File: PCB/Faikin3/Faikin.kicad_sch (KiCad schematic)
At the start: 28 parts, among them J1 1x5, J2 Prog, Q3 PMF250XNEX, U1 ESP32-PICO-MINI-02, U3 MD8942, U4 Barcode

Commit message: Fix RGB
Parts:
- D2: symbol Device:LED_RBGA -> Device:LED_RGBA
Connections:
- net at R12.1: now also D2.3 (BK); no longer D2.2 (BK)
- net at R6.1: now also D2.2 (GK); no longer D2.3 (GK)
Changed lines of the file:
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@@
     )
   )
-  (symbol (lib_id "Device:LED_RBGA") (at 66.675 139.065 0) (unit 1)
+  (symbol (lib_id "Device:LED_RGBA") (at 66.675 139.065 0) (unit 1)
     (in_bom yes) (on_board yes) (dnp no)
     (property "Reference" "D2" (at 66.675 126.4412 0)

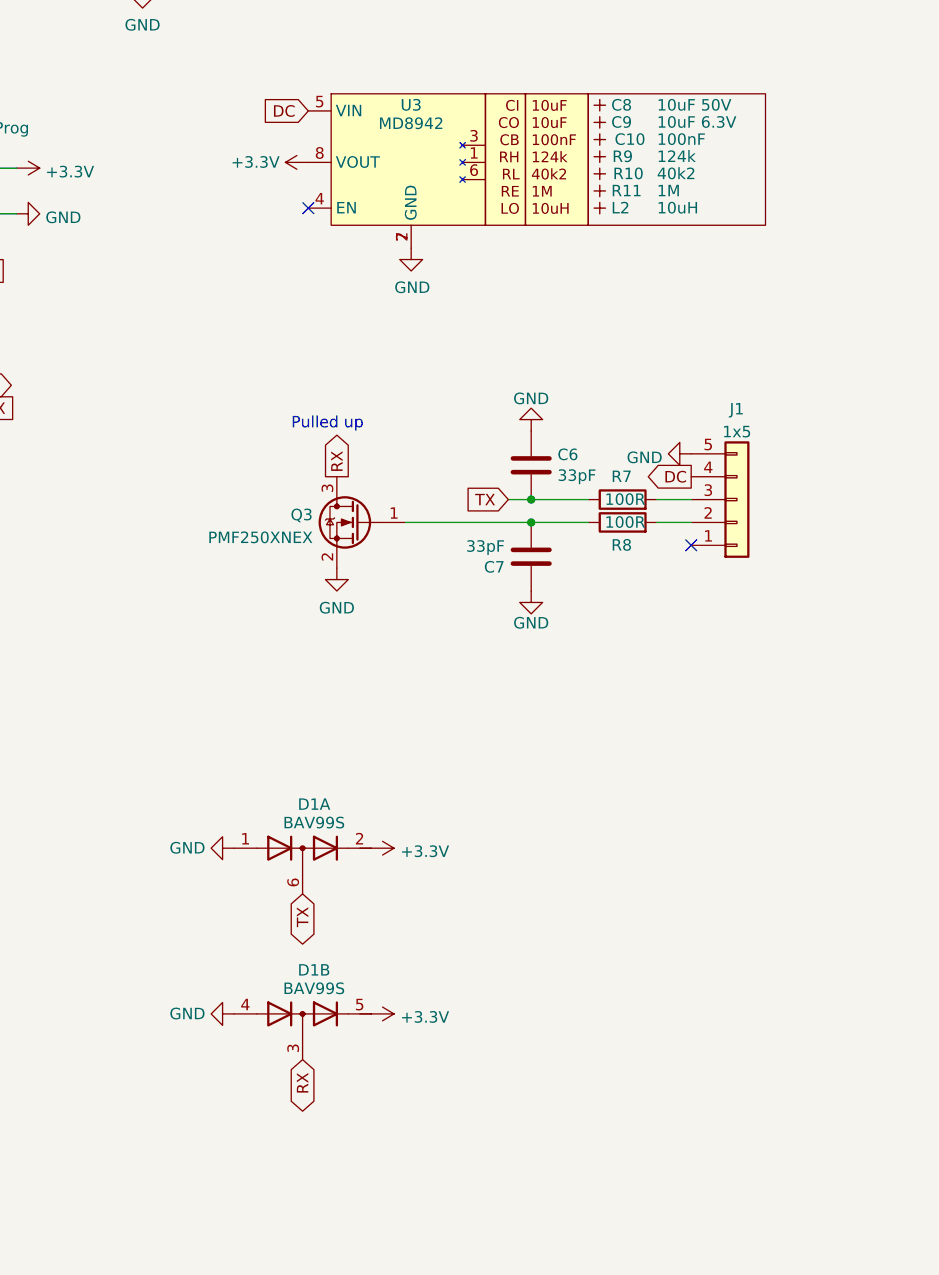
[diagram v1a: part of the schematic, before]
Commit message: Changed to open collector output
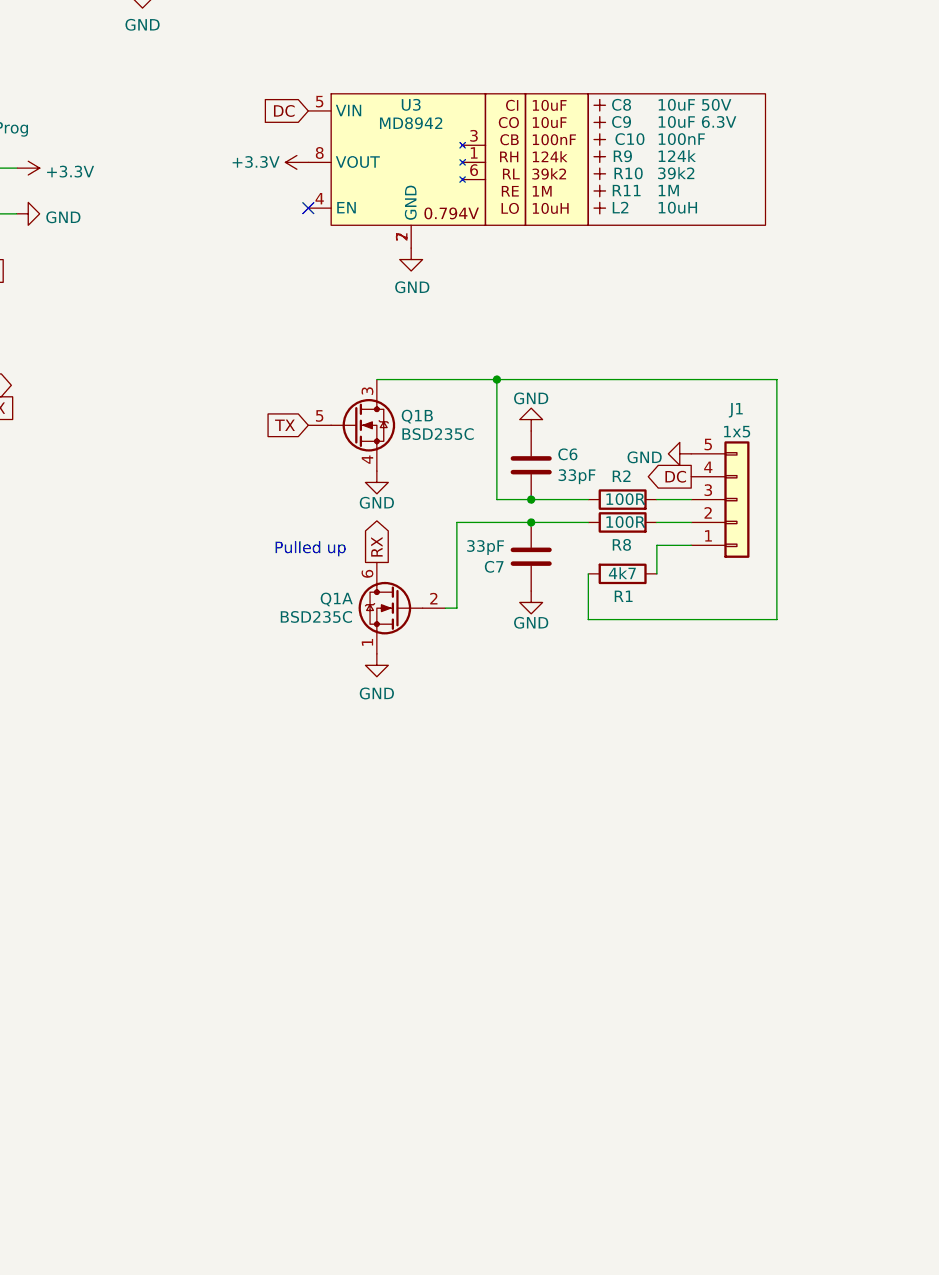
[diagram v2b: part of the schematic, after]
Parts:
- removed D1: BAV99S, RevK:SOT-363_SC-70-6, symbol Diode:BAV99S
- removed Q3: PMF250XNEX, RevK:SOT-323_SC-70, symbol RevK:NX7002AK
- removed R7: 100R, RevK:R_0402, symbol Device:R
- added Q1: BSD235C, RevK:SOT-363_SC-70-6, symbol RevK:BSS138PS
- added R1: 4k7, RevK:R_0402, symbol Device:R
- added R2: 100R, RevK:R_0402, symbol Device:R
- R10: value 40k2 -> 39k2
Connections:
- net GND: now also Q1.1 (SN), Q1.4 (DP)
- net RX: now also Q1.6 (DN)
- net TX: now also Q1.5 (GP); no longer C6.2
- net at C7.2, R8.1: now also Q1.2 (GN)
- net at J1.3 (Pin_3): now also R2.2
- net at J1.1 (Pin_1): now also R1.1
- new net: C6.2, Q1.3 (SP), R1.2, R2.1
- no-connect marks 21 -> 20

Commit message: Fix FET
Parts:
- Q1: value BSD235C -> BSS138PS; JLCPCB Rotation Offset (none) -> 90; LCSC Part # (none) -> C193381
- Q1: value BSD235C -> BSS138PS; LCSC Part # (none) -> C193381
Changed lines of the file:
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@@
       (effects (font (size 1.27 1.27)) (justify left))
     )
-    (property "Value" "BSD235C" (at 129.032 81.669 0)
+    (property "Value" "BSS138PS" (at 129.032 81.669 0)
       (effects (font (size 1.27 1.27)) (justify left))
     )
@@
     (property "Datasheet" "https://datasheet.lcsc.com/lcsc/1810011113_Nexperia-BSS138PS-115_C193381.pdf" (at 123.825 67.31 0)
       (effects (font (size 1.27 1.27)) hide)
+    )
+    (property "LCSC Part #" "C193381" (at 133.35 74.676 0)
+      (effects (font (size 1.27 1.27)) hide)
+    )
+    (property "JLCPCB Rotation Offset" "90" (at 123.825 80.645 0)
+      (effects (font (size 1.27 1.27)))
     )
     (pin "1")
@@
       (effects (font (size 1.27 1.27)) (justify left))
     )
-    (property "Value" "BSD235C" (at 123.698 101.989 0)
+    (property "Value" "BSS138PS" (at 123.698 101.989 0)
       (effects (font (size 1.27 1.27)) (justify left))
     )
@@
       (effects (font (size 1.27 1.27)) hide)
     )
+    (property "LCSC Part #" "C193381" (at 119.38 94.996 0)
+      (effects (font (size 1.27 1.27)) hide)
+    )

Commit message: Silk tidy
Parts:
- removed U4: Barcode, RevK:EAN-5060634238151, symbol RevK:Barcode
- added C2: 100nF, RevK:C_0402, symbol Device:C
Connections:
- net +3.3V: now also C2.1
- net GND: now also C2.2
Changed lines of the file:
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@@
     )
   )
-  (symbol (lib_id "RevK:Barcode") (at 273.05 174.625 0) (unit 1)
-    (in_bom no) (on_board yes) (dnp no) (fields_autoplaced)
-    (property "Reference" "U4" (at 273.05 177.8 0)
-      (effects (font (size 1.27 1.27)) hide)
-    )
-    (property "Value" "Barcode" (at 273.05 179.705 0)
-      (effects (font (size 1.27 1.27)) hide)
-    )
-    (property "Footprint" "RevK:EAN-5060634238151" (at 272.415 175.26 0)
-      (effects (font (size 1.27 1.27)) hide)
-    )
-    (property "Datasheet" "" (at 272.415 175.26 0)
-      (effects (font (size 1.27 1.27)) hide)
-    )
-    (property "Note" "Non part, PCB printed" (at 273.05 168.91 0)
-      (effects (font (size 1.27 1.27)) hide)
-    )
-    (instances
-      (project "Faikin"
-        (path "/46c350bb-7de4-4e81-aafd-4af55e37aab0"
-          (reference "U4") (unit 1)
+  (symbol (lib_id "Device:C") (at 99.695 72.39 0) (unit 1)
+    (in_bom yes) (on_board yes) (dnp no) (fields_autoplaced)
+    (property "Reference" "C2" (at 102.616 71.5553 0)
+      (effects (font (size 1.27 1.27)) (justify left))
+    )
+    (property "Value" "100nF" (at 102.616 74.0922 0)
+      (effects (font (size 1.27 1.27)) (justify left))
+    )
+    (property "Footprint" "RevK:C_0402" (at 100.6602 76.2 0)
+      (effects (font (size 1.27 1.27)) hide)
+    )
+    (property "Datasheet" "~" (at 99.695 72.39 0)
+      (effects (font (size 1.27 1.27)) hide)
+    )
+    (pin "1")
+    (pin "2")
+    (instances
+      (project "Faikin"
+        (path "/46c350bb-7de4-4e81-aafd-4af55e37aab0"
+          (reference "C2") (unit 1)
         )
       )
@@
         (path "/46c350bb-7de4-4e81-aafd-4af55e37aab0"
           (reference "Q1") (unit 2)
+        )
+      )
+    )
+  )
+  (symbol (lib_id "power:GND") (at 99.695 76.2 0) (unit 1)
+    (in_bom yes) (on_board yes) (dnp no) (fields_autoplaced)
+    (property "Reference" "#PWR05" (at 99.695 82.55 0)
+      (effects (font (size 1.27 1.27)) hide)
+    )
+    (property "Value" "GND" (at 99.695 80.6434 0)
+      (effects (font (size 1.27 1.27)))
+    )
+    (property "Footprint" "" (at 99.695 76.2 0)
+      (effects (font (size 1.27 1.27)) hide)
+    )
+    (property "Datasheet" "" (at 99.695 76.2 0)
+      (effects (font (size 1.27 1.27)) hide)
+    )
+    (pin "1")
+    (instances
+      (project "Faikin"
+        (path "/46c350bb-7de4-4e81-aafd-4af55e37aab0"
+          (reference "#PWR05") (unit 1)
         )
       )
@@
         )
       )
+    )
+  )
+  (symbol (lib_id "power:+3.3V") (at 99.695 68.58 0) (unit 1)
+    (in_bom yes) (on_board yes) (dnp no) (fields_autoplaced)
+    (property "Reference" "#PWR04" (at 99.695 72.39 0)
+      (effects (font (size 1.27 1.27)) hide)
+    )
+    (property "Value" "+3.3V" (at 99.695 65.0042 0)
+      (effects (font (size 1.27 1.27)))
+    )
+    (property "Footprint" "" (at 99.695 68.58 0)
+      (effects (font (size 1.27 1.27)) hide)
+    )
+    (property "Datasheet" "" (at 99.695 68.58 0)
+      (effects (font (size 1.27 1.27)) hide)
+    )
+    (pin "1")
+    (instances
+      (project "Faikin"
+        (path "/46c350bb-7de4-4e81-aafd-4af55e37aab0"
+          (reference "#PWR04") (unit 1)
+        )
+      )

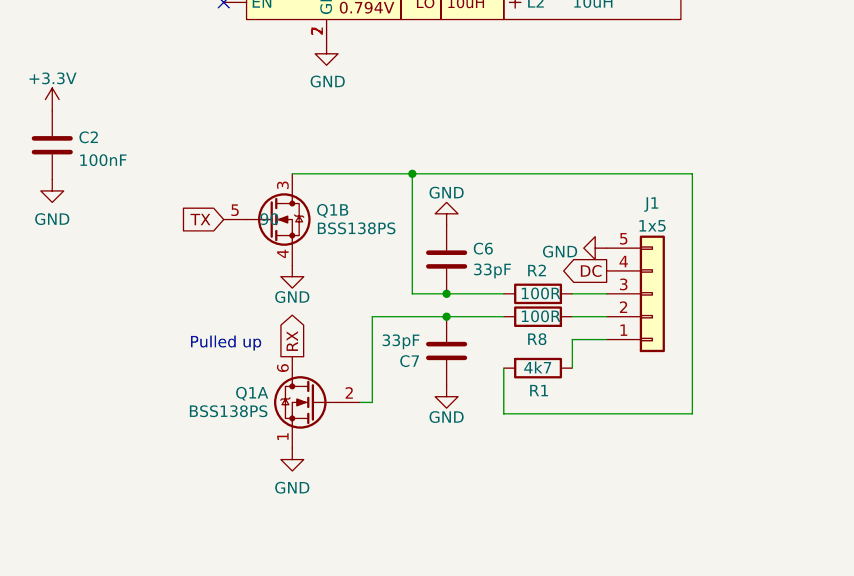
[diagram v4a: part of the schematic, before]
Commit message: Exrta pull up
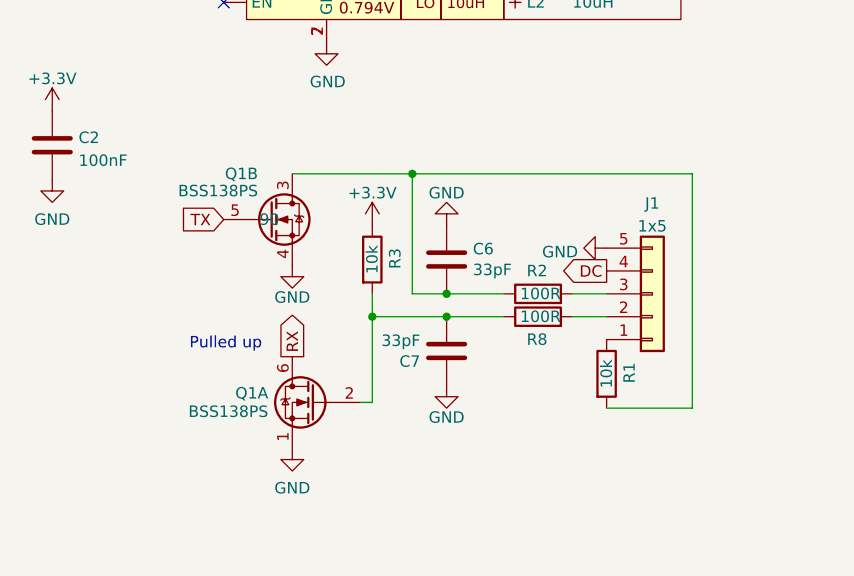
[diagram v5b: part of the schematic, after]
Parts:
- added R3: 10k, RevK:R_0402, symbol Device:R
- R1: value 4k7 -> 10k
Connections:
- net +3.3V: now also R3.1
- net at C7.2, Q1.2 (GN), R8.1: now also R3.2
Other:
- moved on the sheet: R1
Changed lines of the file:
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@@
   (junction (at 81.28 52.07) (diameter 0) (color 0 0 0 0)
+  )
+  (junction (at 135.255 91.44) (diameter 0) (color 0 0 0 0)
   )
   (junction (at 139.7 75.565) (diameter 0) (color 0 0 0 0)
@@
     (stroke (width 0) (type default))
   )
-  (wire (pts (xy 170.815 102.235) (xy 149.86 102.235))
-    (stroke (width 0) (type default))
-  )
   (wire (pts (xy 143.51 91.44) (xy 149.86 91.44))
     (stroke (width 0) (type default))
@@
     (stroke (width 0) (type default))
   )
-  (wire (pts (xy 161.29 93.98) (xy 157.48 93.98))
-    (stroke (width 0) (type default))
-  )
   (wire (pts (xy 126.365 75.565) (xy 139.7 75.565))
     (stroke (width 0) (type default))
@@
     (stroke (width 0) (type default))
   )
-  (wire (pts (xy 135.255 100.965) (xy 135.255 91.44))
-    (stroke (width 0) (type default))
-  )
-  (wire (pts (xy 149.86 102.235) (xy 149.86 97.155))
+  (wire (pts (xy 135.255 91.44) (xy 135.255 100.965))
+    (stroke (width 0) (type default))
+  )
+  (wire (pts (xy 161.29 101.6) (xy 170.815 101.6))
     (stroke (width 0) (type default))
   )
@@
     (stroke (width 0) (type default))
   )
-  (wire (pts (xy 170.815 75.565) (xy 170.815 102.235))
+  (wire (pts (xy 170.815 75.565) (xy 170.815 101.6))
     (stroke (width 0) (type default))
   )
@@
     (stroke (width 0) (type default))
   )
+  (wire (pts (xy 135.255 88.9) (xy 135.255 91.44))
+    (stroke (width 0) (type default))
+  )
   (wire (pts (xy 135.255 91.44) (xy 143.51 91.44))
     (stroke (width 0) (type default))
@@
   )
   (wire (pts (xy 143.51 88.9) (xy 149.86 88.9))
-    (stroke (width 0) (type default))
-  )
-  (wire (pts (xy 157.48 93.98) (xy 157.48 97.155))
     (stroke (width 0) (type default))
   )
@@
   )
   (symbol (lib_name "BSS138PS_1") (lib_id "RevK:BSS138PS") (at 123.825 80.645 0) (unit 2)
-    (in_bom yes) (on_board yes) (dnp no) (fields_autoplaced)
-    (property "Reference" "Q1" (at 129.032 79.621 0)
-      (effects (font (size 1.27 1.27)) (justify left))
-    )
-    (property "Value" "BSS138PS" (at 129.032 81.669 0)
-      (effects (font (size 1.27 1.27)) (justify left))
+    (in_bom yes) (on_board yes) (dnp no)
+    (property "Reference" "Q1" (at 122.555 75.565 0)
+      (effects (font (size 1.27 1.27)) (justify right))
+    )
+    (property "Value" "BSS138PS" (at 122.555 77.47 0)
+      (effects (font (size 1.27 1.27)) (justify right))
     )
     (property "Footprint" "RevK:SOT-363_SC-70-6" (at 123.825 94.615 0)
@@
         (path "/46c350bb-7de4-4e81-aafd-4af55e37aab0"
           (reference "R2") (unit 1)
+        )
+      )
+    )
+  )
+  (symbol (lib_id "Device:R") (at 135.255 85.09 0) (unit 1)
+    (in_bom yes) (on_board yes) (dnp no)
+    (property "Reference" "R3" (at 137.795 83.82 90)
+      (effects (font (size 1.27 1.27)) (justify right))
+    )
+    (property "Value" "10k" (at 135.255 85.09 90)
+      (effects (font (size 1.27 1.27)))
+    )
+    (property "Footprint" "RevK:R_0402" (at 133.477 85.09 90)
+      (effects (font (size 1.27 1.27)) hide)
+    )
+    (property "Datasheet" "~" (at 135.255 85.09 0)
+      (effects (font (size 1.27 1.27)) hide)
+    )
+    (pin "1")
+    (pin "2")
+    (instances
+      (project "Faikin"
+        (path "/46c350bb-7de4-4e81-aafd-4af55e37aab0"
+          (reference "R3") (unit 1)
+        )
+      )
+    )
+  )
+  (symbol (lib_id "power:+3.3V") (at 135.255 81.28 0) (unit 1)
+    (in_bom yes) (on_board yes) (dnp no) (fields_autoplaced)
+    (property "Reference" "#PWR06" (at 135.255 85.09 0)
+      (effects (font (size 1.27 1.27)) hide)
+    )
+    (property "Value" "+3.3V" (at 135.255 77.7042 0)
+      (effects (font (size 1.27 1.27)))
+    )
+    (property "Footprint" "" (at 135.255 81.28 0)
+      (effects (font (size 1.27 1.27)) hide)
+    )
+    (property "Datasheet" "" (at 135.255 81.28 0)
+      (effects (font (size 1.27 1.27)) hide)
+    )
+    (pin "1")
+    (instances
+      (project "Faikin"
+        (path "/46c350bb-7de4-4e81-aafd-4af55e37aab0"
+          (reference "#PWR06") (unit 1)
         )
       )
@@
     )
   )
-  (symbol (lib_id "Device:R") (at 153.67 97.155 270) (unit 1)
-    (in_bom yes) (on_board yes) (dnp no)
-    (property "Reference" "R1" (at 154.94 99.695 90)
+  (symbol (lib_id "Device:R") (at 161.29 97.79 0) (unit 1)
+    (in_bom yes) (on_board yes) (dnp no)
+    (property "Reference" "R1" (at 163.83 96.52 90)
       (effects (font (size 1.27 1.27)) (justify right))
     )
-    (property "Value" "4k7" (at 153.67 97.155 90)
-      (effects (font (size 1.27 1.27)))
-    )
-    (property "Footprint" "RevK:R_0402" (at 153.67 95.377 90)
-      (effects (font (size 1.27 1.27)) hide)
-    )
-    (property "Datasheet" "~" (at 153.67 97.155 0)
-      (effects (font (size 1.27 1.27)) hide)
-    )
+    (property "Value" "10k" (at 161.29 97.79 90)
+      (effects (font (size 1.27 1.27)))
+    )
+    (property "Footprint" "RevK:R_0402" (at 159.512 97.79 90)
+      (effects (font (size 1.27 1.27)) hide)
+    )
+    (property "Datasheet" "~" (at 161.29 97.79 0)
+      (effects (font (size 1.27 1.27)) hide)
+    )

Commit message: Silk
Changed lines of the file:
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@@
     )
     (property "JLCPCB Rotation Offset" "90" (at 123.825 80.645 0)
-      (effects (font (size 1.27 1.27)))
+      (effects (font (size 1.27 1.27)) hide)
     )
     (pin "1")

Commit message: Barcode
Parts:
- added U2: Barcode, RevK:EAN-5060634238151, symbol RevK:Barcode
- Q1: JLCPCB Rotation Offset 90 -> -90
- Q1: JLCPCB Rotation Offset (none) -> -90
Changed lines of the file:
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@@
       (effects (font (size 1.27 1.27)) hide)
     )
-    (property "JLCPCB Rotation Offset" "90" (at 123.825 80.645 0)
+    (property "JLCPCB Rotation Offset" "-90" (at 123.825 80.645 0)
       (effects (font (size 1.27 1.27)) hide)
     )
@@
       (effects (font (size 1.27 1.27)) hide)
     )
+    (property "JLCPCB Rotation Offset" "-90" (at 128.905 100.965 0)
+      (effects (font (size 1.27 1.27)) hide)
+    )
     (pin "1")
     (pin "2")
@@
         )
       )
+    )
+  )
+  (symbol (lib_id "RevK:Barcode") (at 273.05 174.625 0) (unit 1)
+    (in_bom no) (on_board yes) (dnp no) (fields_autoplaced)
+    (property "Reference" "U2" (at 273.05 177.8 0)
+      (effects (font (size 1.27 1.27)) hide)
+    )
+    (property "Value" "Barcode" (at 273.05 179.705 0)
+      (effects (font (size 1.27 1.27)) hide)
+    )
+    (property "Footprint" "RevK:EAN-5060634238151" (at 272.415 175.26 0)
+      (effects (font (size 1.27 1.27)) hide)
+    )
+    (property "Datasheet" "" (at 272.415 175.26 0)
+      (effects (font (size 1.27 1.27)) hide)
+    )
+    (property "Note" "Non part, PCB printed" (at 273.05 168.91 0)
+      (effects (font (size 1.27 1.27)) hide)
+    )
+    (instances
+      (project "Faikin"
+        (path "/46c350bb-7de4-4e81-aafd-4af55e37aab0"
+          (reference "U2") (unit 1)
+        )
+      )
